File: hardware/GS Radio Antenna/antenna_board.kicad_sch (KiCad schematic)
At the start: 22 parts, among them J1 Conn_01x02_Socket, U10 IRF4905PBF, U11 IRF4905PBF, U12 IRF4905PBF, U2 ESP32-DEVKITC, U3 LM3940IT-3.3/NOPB, U4 TLC5916IN, U5 TLC5916IN, U6 TLC5916IN, U9 IRF4905PBF

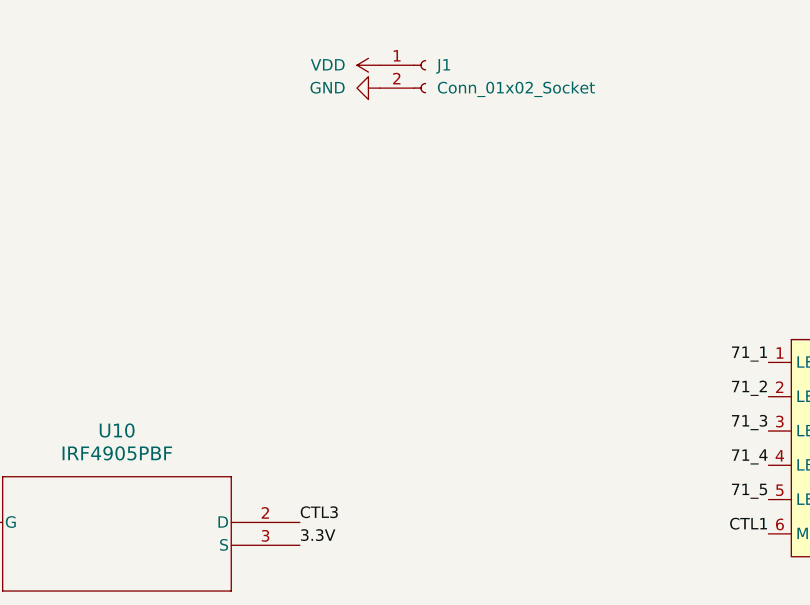
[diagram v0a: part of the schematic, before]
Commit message: New GS Radio board layout without wiring
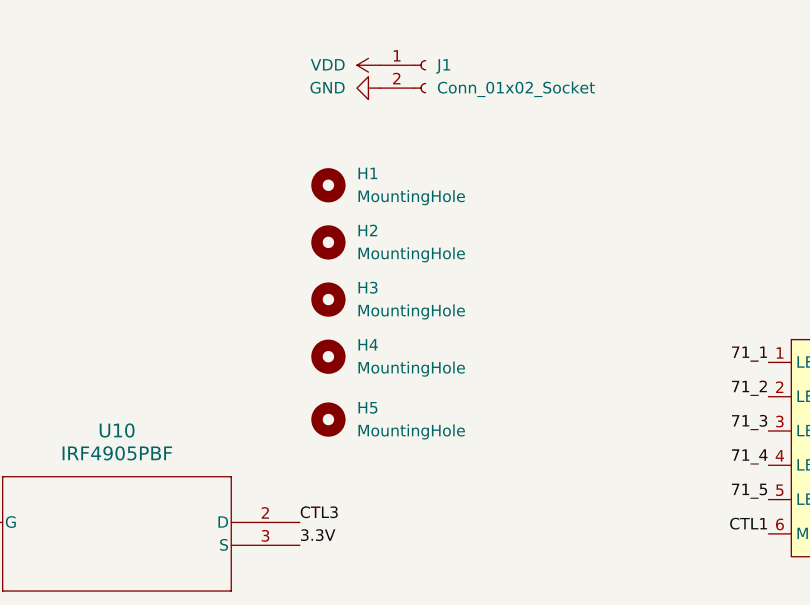
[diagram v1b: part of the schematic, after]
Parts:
- added H1, H2, H3, H4, H5: MountingHole, MountingHole:MountingHole_3.2mm_M3_DIN965_Pad_TopBottom, symbol Mechanical:MountingHole
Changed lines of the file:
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@@
+    )
+  )
+  (symbol (lib_id "Mechanical:MountingHole") (at 146.685 97.155 0) (unit 1)
+    (in_bom yes) (on_board yes) (dnp no) (fields_autoplaced)
+    (property "Reference" "H1" (at 149.86 95.885 0)
+      (effects (font (size 1.27 1.27)) (justify left))
+    )
+    (property "Value" "MountingHole" (at 149.86 98.425 0)
+      (effects (font (size 1.27 1.27)) (justify left))
+    )
+    (property "Footprint" "MountingHole:MountingHole_3.2mm_M3_DIN965_Pad_TopBottom" (at 146.685 97.155 0)
+      (effects (font (size 1.27 1.27)) hide)
+    )
+    (property "Datasheet" "~" (at 146.685 97.155 0)
+      (effects (font (size 1.27 1.27)) hide)
+    )
+    (instances
+      (project "antenna_board"
+        (path "/61096121-d89e-4ff3-b26c-bc940a13f838"
+          (reference "H1") (unit 1)
+        )
+      )
     )
   )
@@
     )
   )
+  (symbol (lib_id "Mechanical:MountingHole") (at 146.685 109.855 0) (unit 1)
+    (in_bom yes) (on_board yes) (dnp no) (fields_autoplaced)
+    (property "Reference" "H3" (at 149.86 108.585 0)
+      (effects (font (size 1.27 1.27)) (justify left))
+    )
+    (property "Value" "MountingHole" (at 149.86 111.125 0)
+      (effects (font (size 1.27 1.27)) (justify left))
+    )
+    (property "Footprint" "MountingHole:MountingHole_3.2mm_M3_DIN965_Pad_TopBottom" (at 146.685 109.855 0)
+      (effects (font (size 1.27 1.27)) hide)
+    )
+    (property "Datasheet" "~" (at 146.685 109.855 0)
+      (effects (font (size 1.27 1.27)) hide)
+    )
+    (instances
+      (project "antenna_board"
+        (path "/61096121-d89e-4ff3-b26c-bc940a13f838"
+          (reference "H3") (unit 1)
+        )
+      )
+    )
+  )
   (symbol (lib_id "IRF4905:IRF4905PBF_1") (at 35.56 134.62 0) (unit 1)
     (in_bom yes) (on_board yes) (dnp no) (fields_autoplaced)
@@
     )
   )
+  (symbol (lib_id "Mechanical:MountingHole") (at 146.685 103.505 0) (unit 1)
+    (in_bom yes) (on_board yes) (dnp no) (fields_autoplaced)
+    (property "Reference" "H2" (at 149.86 102.235 0)
+      (effects (font (size 1.27 1.27)) (justify left))
+    )
+    (property "Value" "MountingHole" (at 149.86 104.775 0)
+      (effects (font (size 1.27 1.27)) (justify left))
+    )
+    (property "Footprint" "MountingHole:MountingHole_3.2mm_M3_DIN965_Pad_TopBottom" (at 146.685 103.505 0)
+      (effects (font (size 1.27 1.27)) hide)
+    )
+    (property "Datasheet" "~" (at 146.685 103.505 0)
+      (effects (font (size 1.27 1.27)) hide)
+    )
+    (instances
+      (project "antenna_board"
+        (path "/61096121-d89e-4ff3-b26c-bc940a13f838"
+          (reference "H2") (unit 1)
+        )
+      )
+    )
+  )
   (symbol (lib_id "Device:R") (at 193.04 53.34 90) (unit 1)
     (in_bom yes) (on_board yes) (dnp no) (fields_autoplaced)
@@
         (path "/61096121-d89e-4ff3-b26c-bc940a13f838"
           (reference "#PWR03") (unit 1)
+        )
+      )
+    )
+  )
+  (symbol (lib_id "Mechanical:MountingHole") (at 146.685 123.19 0) (unit 1)
+    (in_bom yes) (on_board yes) (dnp no) (fields_autoplaced)
+    (property "Reference" "H5" (at 149.86 121.92 0)
+      (effects (font (size 1.27 1.27)) (justify left))
+    )
+    (property "Value" "MountingHole" (at 149.86 124.46 0)
+      (effects (font (size 1.27 1.27)) (justify left))
+    )
+    (property "Footprint" "MountingHole:MountingHole_3.2mm_M3_DIN965_Pad_TopBottom" (at 146.685 123.19 0)
+      (effects (font (size 1.27 1.27)) hide)
+    )
+    (property "Datasheet" "~" (at 146.685 123.19 0)
+      (effects (font (size 1.27 1.27)) hide)
+    )
+    (instances
+      (project "antenna_board"
+        (path "/61096121-d89e-4ff3-b26c-bc940a13f838"
+          (reference "H5") (unit 1)
         )
       )
@@
         )
       )
+    )
+  )
+  (symbol (lib_id "Mechanical:MountingHole") (at 146.685 116.205 0) (unit 1)
+    (in_bom yes) (on_board yes) (dnp no) (fields_autoplaced)
+    (property "Reference" "H4" (at 149.86 114.935 0)
+      (effects (font (size 1.27 1.27)) (justify left))
+    )
+    (property "Value" "MountingHole" (at 149.86 117.475 0)
+      (effects (font (size 1.27 1.27)) (justify left))
+    )
+    (property "Footprint" "MountingHole:MountingHole_3.2mm_M3_DIN965_Pad_TopBottom" (at 146.685 116.205 0)
+      (effects (font (size 1.27 1.27)) hide)
+    )
+    (property "Datasheet" "~" (at 146.685 116.205 0)
+      (effects (font (size 1.27 1.27)) hide)
+    )
+    (instances
+      (project "antenna_board"
+        (path "/61096121-d89e-4ff3-b26c-bc940a13f838"
+          (reference "H4") (unit 1)
+        )
+      )

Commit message: Finished GS Radio layout
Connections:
- net GND: now also U2.14 (GND1), U2.32 (GND2), U2.38 (GND3)
- net SCK: no longer U4.3 (CLK), U5.3 (CLK), U6.3 (CLK)
- net CLK: now reaches U2.31 (IO19)
- net CLK: now also U4.3 (CLK), U5.3 (CLK), U6.3 (CLK)
- no-connect marks 39 -> 35
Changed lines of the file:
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@@
   (no_connect (at 27.94 104.14))
   (no_connect (at 68.58 106.68))
-  (no_connect (at 27.94 93.98))
   (no_connect (at 68.58 104.14))
   (no_connect (at 68.58 91.44))
@@
   (no_connect (at 27.94 99.06))
   (no_connect (at 102.87 87.63))
-  (no_connect (at 68.58 76.2))
   (no_connect (at 276.86 48.26))
   (no_connect (at 177.8 38.1))
   (no_connect (at 27.94 73.66))
-  (no_connect (at 68.58 78.74))
   (no_connect (at 68.58 101.6))
   (no_connect (at 68.58 86.36))
-  (no_connect (at 68.58 60.96))
   (no_connect (at 83.82 87.63))
   (wire (pts (xy 93.98 134.62) (xy 97.79 134.62))
@@
     (effects (font (size 1.27 1.27)) (justify left bottom))
   )
-  (label "SCK" (at 142.24 30.48 180) (fields_autoplaced)
+  (label "CLK" (at 142.24 30.48 180) (fields_autoplaced)
     (effects (font (size 1.27 1.27)) (justify right bottom))
   )
@@
     (effects (font (size 1.27 1.27)) (justify right bottom))
   )
-  (label "SCK" (at 241.3 30.48 180) (fields_autoplaced)
+  (label "CLK" (at 241.3 30.48 180) (fields_autoplaced)
     (effects (font (size 1.27 1.27)) (justify right bottom))
   )
@@
     (effects (font (size 1.27 1.27)) (justify right bottom))
   )
+  (label "CLK" (at 68.58 78.74 0) (fields_autoplaced)
+    (effects (font (size 1.27 1.27)) (justify left bottom))
+  )
   (label "72_1" (at 233.68 116.84 180) (fields_autoplaced)
     (effects (font (size 1.27 1.27)) (justify right bottom))
@@
     (effects (font (size 1.27 1.27)) (justify left bottom))
   )
-  (label "SCK" (at 196.85 30.48 180) (fields_autoplaced)
+  (label "CLK" (at 196.85 30.48 180) (fields_autoplaced)
     (effects (font (size 1.27 1.27)) (justify right bottom))
   )
@@
     )
   )
+  (symbol (lib_id "power:GND") (at 68.58 76.2 90) (unit 1)
+    (in_bom yes) (on_board yes) (dnp no) (fields_autoplaced)
+    (property "Reference" "#PWR015" (at 74.93 76.2 0)
+      (effects (font (size 1.27 1.27)) hide)
+    )
+    (property "Value" "GND" (at 71.755 76.2 90)
+      (effects (font (size 1.27 1.27)) (justify right))
+    )
+    (property "Footprint" "" (at 68.58 76.2 0)
+      (effects (font (size 1.27 1.27)) hide)
+    )
+    (property "Datasheet" "" (at 68.58 76.2 0)
+      (effects (font (size 1.27 1.27)) hide)
+    )
+    (pin "1")
+    (instances
+      (project "antenna_board"
+        (path "/61096121-d89e-4ff3-b26c-bc940a13f838"
+          (reference "#PWR015") (unit 1)
+        )
+      )
+    )
+  )
   (symbol (lib_id "IRF4905:IRF4905PBF_1") (at 102.87 134.62 0) (unit 1)
     (in_bom yes) (on_board yes) (dnp no) (fields_autoplaced)
@@
     )
   )
+  (symbol (lib_id "power:GND") (at 27.94 93.98 270) (unit 1)
+    (in_bom yes) (on_board yes) (dnp no) (fields_autoplaced)
+    (property "Reference" "#PWR016" (at 21.59 93.98 0)
+      (effects (font (size 1.27 1.27)) hide)
+    )
+    (property "Value" "GND" (at 24.13 93.98 90)
+      (effects (font (size 1.27 1.27)) (justify right))
+    )
+    (property "Footprint" "" (at 27.94 93.98 0)
+      (effects (font (size 1.27 1.27)) hide)
+    )
+    (property "Datasheet" "" (at 27.94 93.98 0)
+      (effects (font (size 1.27 1.27)) hide)
+    )
+    (pin "1")
+    (instances
+      (project "antenna_board"
+        (path "/61096121-d89e-4ff3-b26c-bc940a13f838"
+          (reference "#PWR016") (unit 1)
+        )
+      )
+    )
+  )
   (symbol (lib_id "power:GND") (at 134.62 53.34 270) (unit 1)
     (in_bom yes) (on_board yes) (dnp no) (fields_autoplaced)
@@
         )
       )
+    )
+  )
+  (symbol (lib_id "power:GND") (at 68.58 60.96 90) (unit 1)
+    (in_bom yes) (on_board yes) (dnp no) (fields_autoplaced)
+    (property "Reference" "#PWR014" (at 74.93 60.96 0)
+      (effects (font (size 1.27 1.27)) hide)
+    )
+    (property "Value" "GND" (at 71.755 60.96 90)
+      (effects (font (size 1.27 1.27)) (justify right))
+    )
+    (property "Footprint" "" (at 68.58 60.96 0)
+      (effects (font (size 1.27 1.27)) hide)
+    )
+    (property "Datasheet" "" (at 68.58 60.96 0)
+      (effects (font (size 1.27 1.27)) hide)
+    )
+    (pin "1")
+    (instances
+      (project "antenna_board"
+        (path "/61096121-d89e-4ff3-b26c-bc940a13f838"
+          (reference "#PWR014") (unit 1)
+        )
+      )

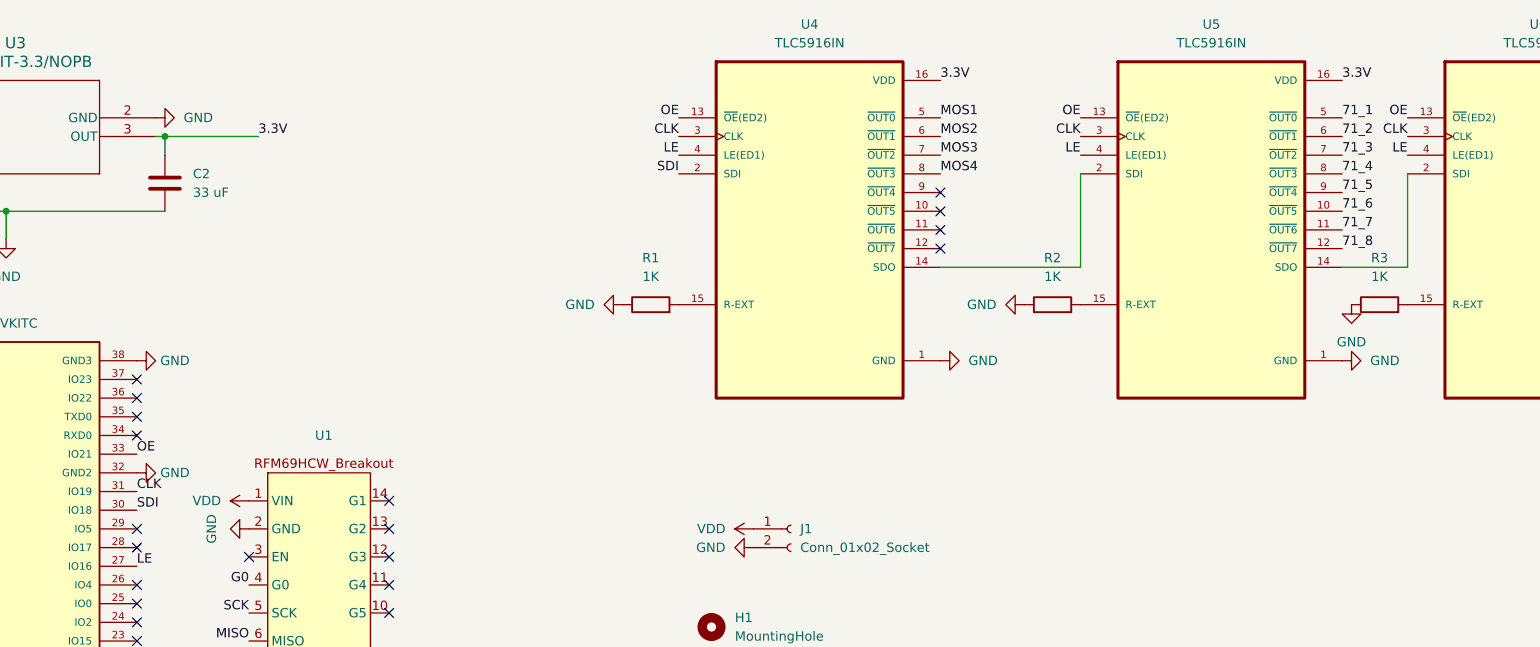
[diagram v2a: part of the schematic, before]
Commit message: Add logo and switch displays to HSPI radio
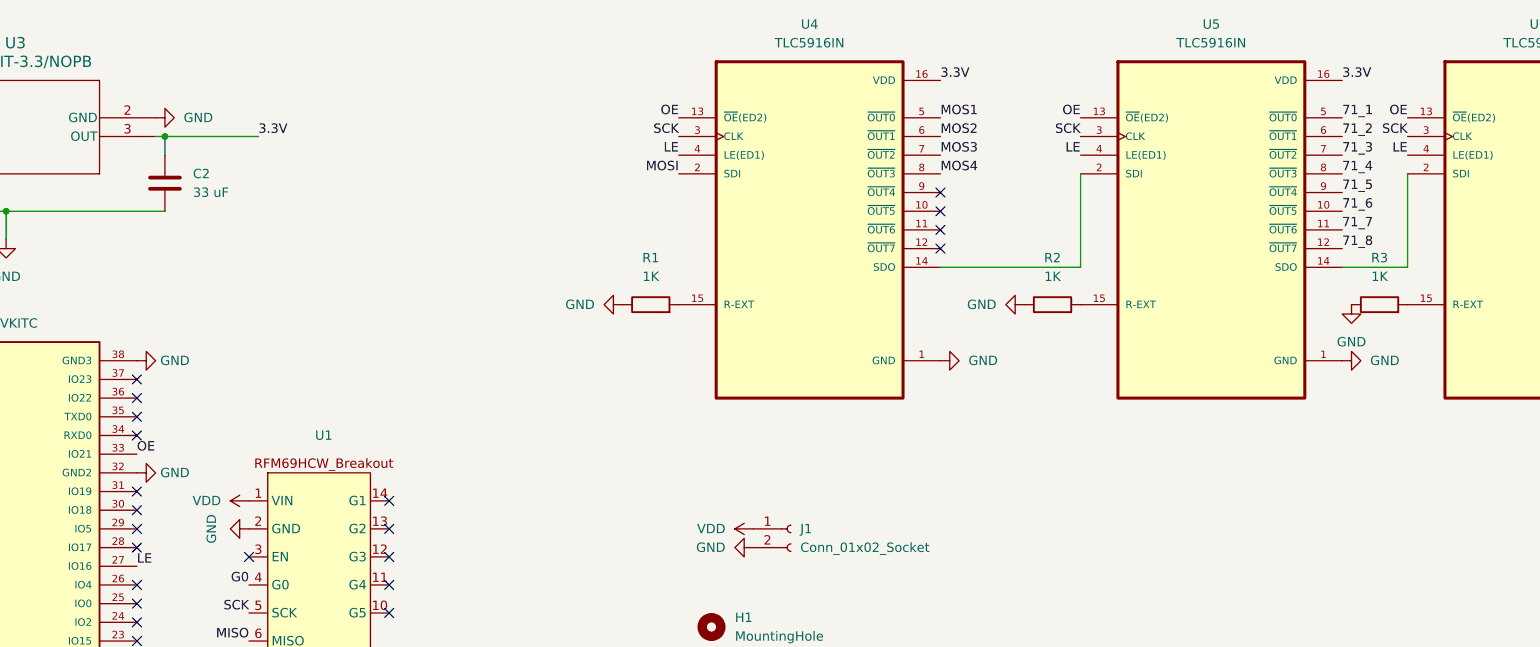
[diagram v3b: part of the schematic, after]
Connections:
- net MOSI: now also U4.2 (SDI)
- net SCK: now also U4.3 (CLK), U5.3 (CLK), U6.3 (CLK)
- removed net CLK: U2.31 (IO19), U4.3 (CLK), U5.3 (CLK), U6.3 (CLK)
- net SDI: no longer names the net of U2.30 (IO18)
- net SDI: no longer U4.2 (SDI)
- no-connect marks 35 -> 37
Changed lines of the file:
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@@
   (no_connect (at 68.58 66.04))
   (no_connect (at 27.94 68.58))
+  (no_connect (at 68.58 78.74))
   (no_connect (at 27.94 101.6))
   (no_connect (at 177.8 43.18))
@@
   (no_connect (at 177.8 40.64))
   (no_connect (at 68.58 99.06))
+  (no_connect (at 68.58 81.28))
   (no_connect (at 27.94 76.2))
   (no_connect (at 27.94 99.06))
@@
     (effects (font (size 1.27 1.27)) (justify left bottom))
   )
-  (label "CLK" (at 142.24 30.48 180) (fields_autoplaced)
+  (label "SCK" (at 142.24 30.48 180) (fields_autoplaced)
     (effects (font (size 1.27 1.27)) (justify right bottom))
   )
@@
     (effects (font (size 1.27 1.27)) (justify right bottom))
   )
-  (label "SDI" (at 142.24 35.56 180) (fields_autoplaced)
-    (effects (font (size 1.27 1.27)) (justify right bottom))
-  )
-  (label "CLK" (at 241.3 30.48 180) (fields_autoplaced)
+  (label "MOSI" (at 142.24 35.56 180) (fields_autoplaced)
+    (effects (font (size 1.27 1.27)) (justify right bottom))
+  )
+  (label "SCK" (at 241.3 30.48 180) (fields_autoplaced)
     (effects (font (size 1.27 1.27)) (justify right bottom))
   )
@@
     (effects (font (size 1.27 1.27)) (justify right bottom))
   )
-  (label "CLK" (at 68.58 78.74 0) (fields_autoplaced)
-    (effects (font (size 1.27 1.27)) (justify left bottom))
-  )
   (label "72_1" (at 233.68 116.84 180) (fields_autoplaced)
     (effects (font (size 1.27 1.27)) (justify right bottom))
@@
     (effects (font (size 1.27 1.27)) (justify left bottom))
   )
-  (label "CLK" (at 196.85 30.48 180) (fields_autoplaced)
+  (label "SCK" (at 196.85 30.48 180) (fields_autoplaced)
     (effects (font (size 1.27 1.27)) (justify right bottom))
   )
@@
     (effects (font (size 1.27 1.27)) (justify left bottom))
   )
-  (label "SDI" (at 68.58 81.28 0) (fields_autoplaced)
-    (effects (font (size 1.27 1.27)) (justify left bottom))
-  )

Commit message: Changed capacitor
Changed the large capacitor for the voltage regulator to reflect BOM
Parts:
- C2: footprint Capacitor_SMD:C_0603_1608Metric_Pad1.08x0.95mm_HandSolder -> Capacitor_SMD:C_0805_2012Metric_Pad1.18x1.45mm_HandSolder
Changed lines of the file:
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@@
       (effects (font (size 1.27 1.27)) (justify left))
     )
-    (property "Footprint" "Capacitor_SMD:C_0603_1608Metric_Pad1.08x0.95mm_HandSolder" (at 73.3552 40.64 0)
+    (property "Footprint" "Capacitor_SMD:C_0805_2012Metric_Pad1.18x1.45mm_HandSolder" (at 73.3552 40.64 0)
       (effects (font (size 1.27 1.27)) hide)
     )
